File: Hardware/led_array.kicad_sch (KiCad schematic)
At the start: 69 parts, among them U1 74HC595, U10 74HC595, U11 74HC595, U4 74HC595, U6 74HC595, U7 74HC595, U8 74HC595, U9 74HC595

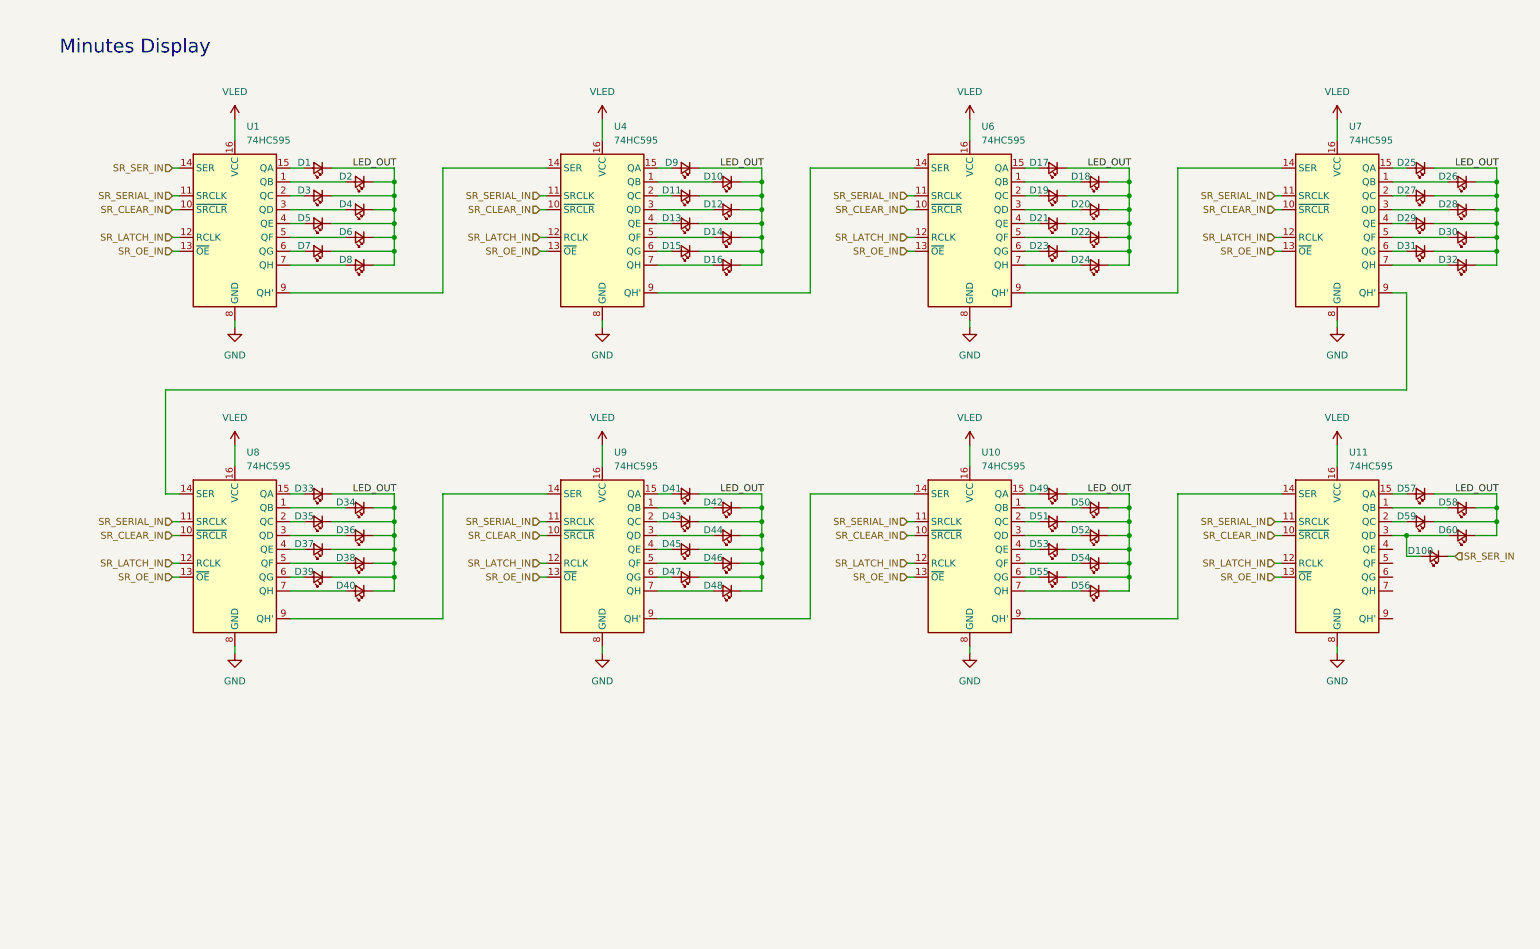
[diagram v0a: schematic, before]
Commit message: semi-final component placements and final component selections. Abandoning due to high routing complexity and need for a 4L board.
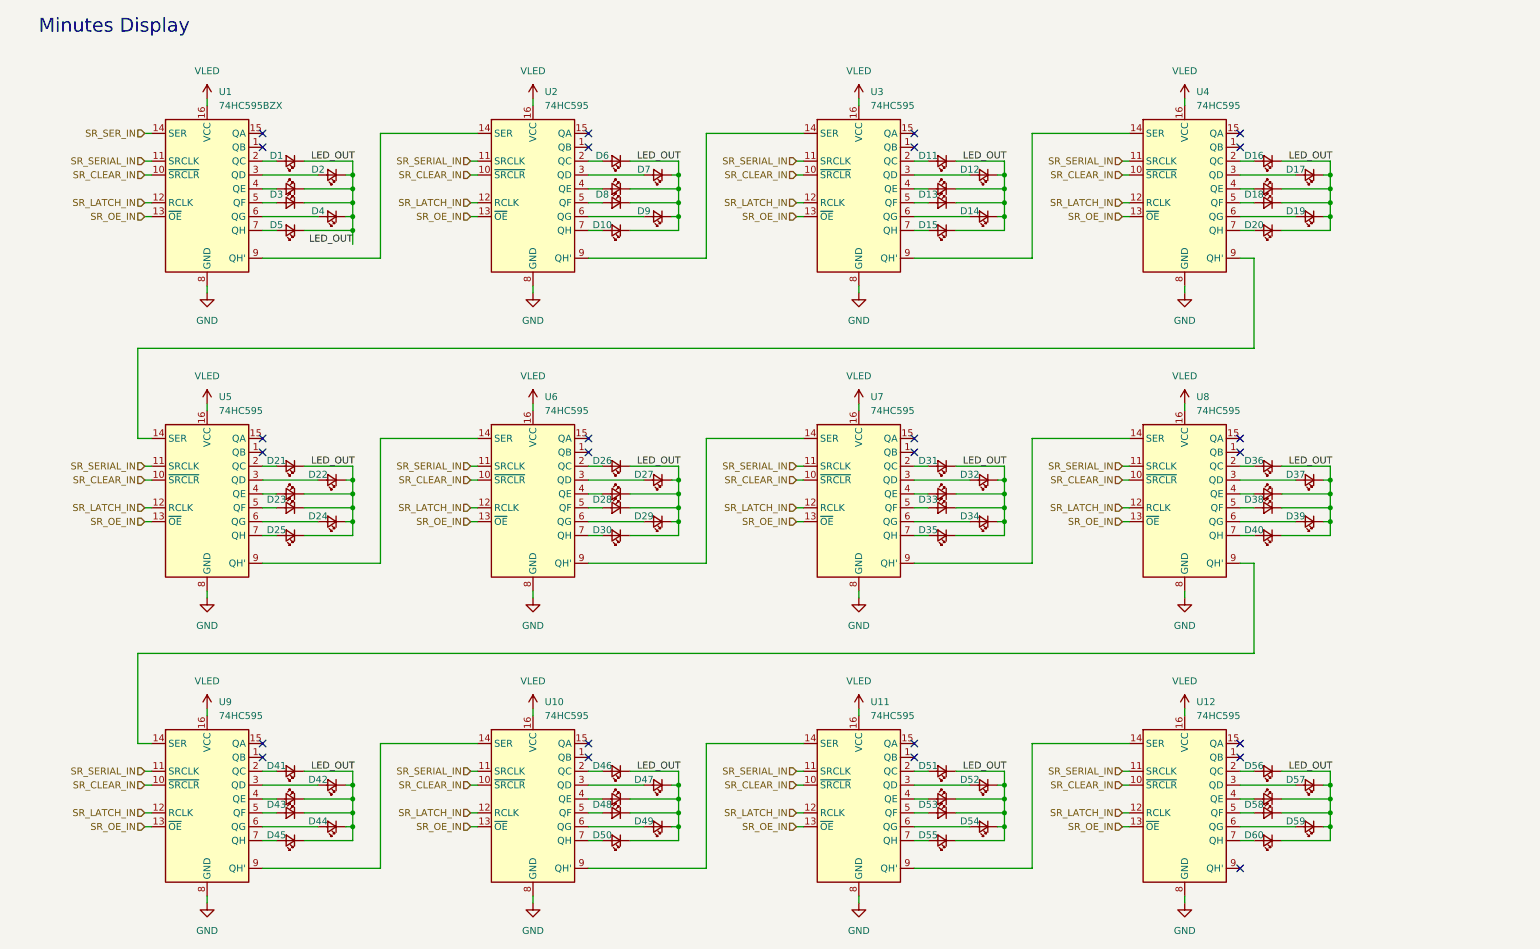
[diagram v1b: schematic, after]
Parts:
- removed D100: LED_Small, symbol Device:LED_Small
- added U12, U2, U3, U5: 74HC595, KiCad:74HC595BZX, symbol 74xx:74HC595
- D1, D10, D11, D12, D14, D15, D16, D17, D19, D2, D20, D21, D22, D24, D25, D26, D27, D29, D30, D31, D32, D34, D35, D36, D37, D39, D4, D40, D41, D42, D44, D45, D46, D47, D49, D5, D50, D51, D52, D54, D55, D56, D57, D59, D6, D60, D7, D9: footprint LED_SMD:LED_0603_1608Metric -> LED_Custom:LED_0603-2
- D13, D18, D23, D28, D3, D33, D38, D43, D48, D53, D58, D8: footprint LED_SMD:LED_0603_1608Metric -> LED_Custom:LED_0603-4
- U1: value 74HC595 -> 74HC595BZX
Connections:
- net GND: now also U1.17 (GND), U10.17 (GND), U11.17 (GND), U4.17 (GND), U6.17 (GND), U7.17 (GND), U8.17 (GND), U9.17 (GND), U12.17 (GND), U12.8 (GND), U2.17 (GND), U2.8 (GND), U3.17 (GND), U3.8 (GND), U5.17 (GND), U5.8 (GND)
- net LED_OUT: now also D13.2 (K), D18.2 (K), D23.2 (K), D28.2 (K), D3.2 (K), D33.2 (K), D38.2 (K), D43.2 (K), D48.2 (K), D53.2 (K), D58.2 (K), D8.2 (K)
- net SR_CLEAR_IN: now also U12.10 (~{SRCLR}), U2.10 (~{SRCLR}), U3.10 (~{SRCLR}), U5.10 (~{SRCLR})
- net SR_LATCH_IN: now also U12.12 (RCLK), U2.12 (RCLK), U3.12 (RCLK), U5.12 (RCLK)
- net SR_OE_IN: now also U12.13 (~{OE}), U2.13 (~{OE}), U3.13 (~{OE}), U5.13 (~{OE})
- net SR_SERIAL_IN: now also U12.11 (SRCLK), U2.11 (SRCLK), U3.11 (SRCLK), U5.11 (SRCLK)
- net VLED: now also U12.16 (VCC), U2.16 (VCC), U3.16 (VCC), U5.16 (VCC)
- net at D17.2 (A): now also U4.3 (QD); no longer U6.15 (QA)
- net at D26.2 (A): now also U6.2 (QC); no longer U7.1 (QB)
- net at U7.15 (QA): no longer D25.2 (A)
- net at U7.2 (QC): now also D31.2 (A); no longer D27.2 (A)
- net at U7.3 (QD): now also D32.2 (A); no longer D28.2 (A)
- net at U7.4 (QE): now also D33.3 (A); no longer D29.2 (A)
- net at U7.5 (QF): now also D33.4 (A); no longer D30.2 (A)
- net at U7.6 (QG): now also D34.2 (A); no longer D31.2 (A)
- net at U7.7 (QH): now also D35.2 (A); no longer D32.2 (A)
- net at D11.2 (A): now also U3.2 (QC); no longer U4.2 (QC)
- net at U10.3 (QD): now also D47.2 (A); no longer D52.2 (A)
- net at U4.7 (QH): now also D20.2 (A); no longer D16.2 (A)
- net at D41.2 (A): now also U9.2 (QC); no longer U9.15 (QA)
- net at D42.2 (A): now also U9.3 (QD); no longer U9.1 (QB)
- net at D44.2 (A): now also U9.6 (QG); no longer U9.3 (QD)
- net at U9.4 (QE): now also D43.3 (A); no longer D45.2 (A)
- net at D46.2 (A): now also U10.2 (QC); no longer U9.5 (QF)
- net at U9.7 (QH): now also D45.2 (A); no longer D48.2 (A)
- net at D24.2 (A): now also U5.6 (QG); no longer U6.7 (QH)
- net at U6.1 (QB): no longer D18.2 (A)
- net at D54.2 (A): now also U11.6 (QG); no longer U10.5 (QF)
- net at D5.2 (A): now also U1.7 (QH); no longer U1.4 (QE)
- net at U11.1 (QB): no longer D58.2 (A)
- net at U4.5 (QF): now also D18.4 (A); no longer D14.2 (A)
- net at D10.2 (A): now also U2.7 (QH); no longer U4.1 (QB)
- net at U10.4 (QE): now also D48.3 (A); no longer D53.2 (A)
- net at D1.2 (A): now also U1.2 (QC); no longer U1.15 (QA)
- net at D60.2 (A): now also U12.7 (QH); no longer U11.3 (QD)
- net at U8.3 (QD): now also D37.2 (A); no longer D36.2 (A)
- net at D12.2 (A): now also U3.3 (QD); no longer U4.3 (QD)
- net at D57.2 (A): now also U12.3 (QD); no longer U11.15 (QA)
- net at U10.6 (QG): now also D49.2 (A); no longer D55.2 (A)
- net at D51.2 (A): now also U11.2 (QC); no longer U10.2 (QC)
- net at D21.2 (A): now also U5.2 (QC); no longer U6.4 (QE)
- net at D15.2 (A): now also U3.7 (QH); no longer U4.6 (QG)
- net at U8.4 (QE): now also D38.3 (A); no longer D37.2 (A)
- net at U10.15 (QA): no longer D49.2 (A)
- net at D9.2 (A): now also U2.6 (QG); no longer U4.15 (QA)
- net at D59.2 (A): now also U12.6 (QG); no longer U11.2 (QC)
- net at U8.2 (QC): now also D36.2 (A); no longer D35.2 (A)
- net at D4.2 (A): now also U1.6 (QG); no longer U1.3 (QD)
- net at D50.2 (A): now also U10.7 (QH); no longer U10.1 (QB)
- net at D56.2 (A): now also U12.2 (QC); no longer U10.7 (QH)
- net at U4.14 (SER): now also U3.9 (QH'); no longer U1.9 (QH')
- net at U4.4 (QE): now also D18.3 (A); no longer D13.2 (A)
- net at U4.9 (QH'): now also U5.14 (SER); no longer U6.14 (SER)
- net at D7.2 (A): now also U2.3 (QD); no longer U1.6 (QG)
- net at U8.1 (QB): no longer D34.2 (A)
- net at U8.15 (QA): no longer D33.2 (A)
- net at U8.5 (QF): now also D38.4 (A); no longer D38.2 (A)
- net at D19.2 (A): now also U4.6 (QG); no longer U6.2 (QC)
- net at U6.3 (QD): now also D27.2 (A); no longer D20.2 (A)
- net at D22.2 (A): now also U5.3 (QD); no longer U6.5 (QF)
- net at U6.6 (QG): now also D29.2 (A); no longer D23.2 (A)
- net at U1.1 (QB): no longer D2.2 (A)
- net at U1.5 (QF): now also D3.4 (A); no longer D6.2 (A)
- net at U11.4 (QE): now also D53.3 (A)
- net at U11.5 (QF): now also D53.4 (A)
- net at U11.7 (QH): now also D55.2 (A)
- net at U11.9 (QH'): now also U12.14 (SER)
- new net: D58.3 (A), U12.4 (QE)
- new net: D58.4 (A), U12.5 (QF)
- new net: D13.3 (A), U3.4 (QE)
- new net: D13.4 (A), U3.5 (QF)
- new net: D3.3 (A), U1.4 (QE)
- new net: D52.2 (A), U11.3 (QD)
- new net: D6.2 (A), U2.2 (QC)
- new net: D30.2 (A), U6.7 (QH)
- new net: U2.9 (QH'), U3.14 (SER)
- new net: D14.2 (A), U3.6 (QG)
- new net: D48.4 (A), U10.5 (QF)
- new net: D8.3 (A), U2.4 (QE)
- new net: D8.4 (A), U2.5 (QF)
- new net: U1.9 (QH'), U2.14 (SER)
- new net: D16.2 (A), U4.2 (QC)
- new net: D43.4 (A), U9.5 (QF)
- new net: D2.2 (A), U1.3 (QD)
- new net: D28.3 (A), U6.4 (QE)
- new net: D28.4 (A), U6.5 (QF)
- new net: D23.3 (A), U5.4 (QE)
- new net: D23.4 (A), U5.5 (QF)
- new net: D25.2 (A), U5.7 (QH)
- new net: U5.9 (QH'), U6.14 (SER)
- no-connect marks 0 -> 25
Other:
- moved on the sheet: D1, D2, D4, D5, U1
